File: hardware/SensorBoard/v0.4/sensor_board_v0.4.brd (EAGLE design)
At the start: 46.8 x 39.9 mm, 59 parts, among them IC1 MCP1703CB, IC2 MCP1703CB, J3 USB-MICROB, Q1 MMBT5088-NPN, U1 ATMEGA328P, U2 TSL2561FN, U4 MPL115A, U5 FT231XS, Y1 16MHZ

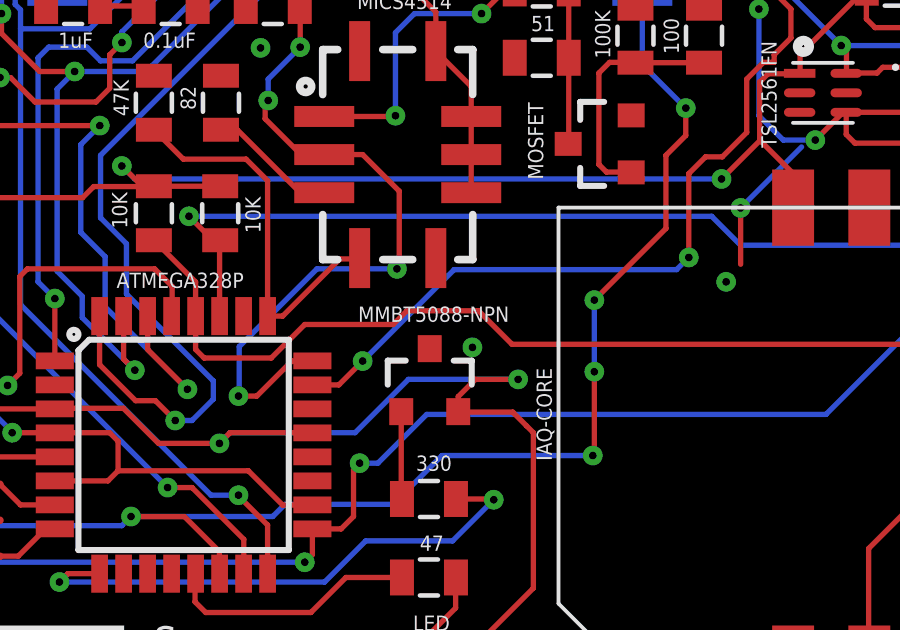
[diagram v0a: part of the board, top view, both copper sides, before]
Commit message: Removed 'label' from SMA connector
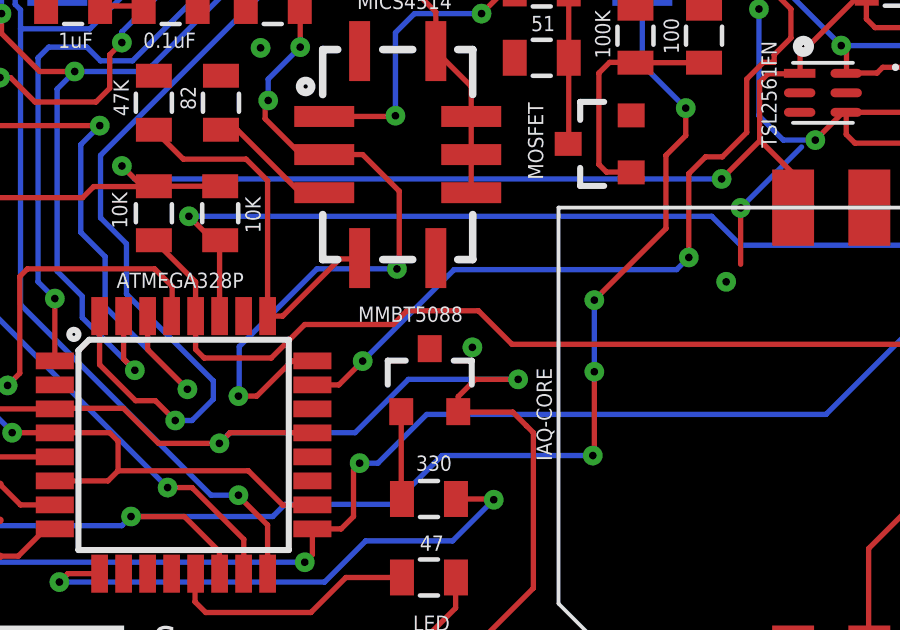
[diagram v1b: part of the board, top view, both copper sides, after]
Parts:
- Q1: value MMBT5088-NPN -> MMBT5088
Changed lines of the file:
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@@
 <attribute name="VALUE" x="30.4546" y="16.4084" size="0.508" layer="121" font="vector" rot="R180"/>
 </element>
-<element name="Q1" library="SparkFun-DiscreteSemi" package="SOT23-3" value="MMBT5088-NPN" x="29.718" y="18.8722" smashed="yes">
+<element name="Q1" library="SparkFun-DiscreteSemi" package="SOT23-3" value="MMBT5088" x="29.718" y="18.8722" smashed="yes">
 <attribute name="PROD_ID" value="TRANS-11160" x="29.718" y="18.8722" size="1.778" layer="27" display="off"/>
 <attribute name="OC_NEWARK" value="unknown" x="29.718" y="18.8722" size="1.778" layer="27" display="off"/>
